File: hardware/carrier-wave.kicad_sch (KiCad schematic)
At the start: 26 parts, among them J1 USB C 2.0, U1 ATSAMD21E18A-M

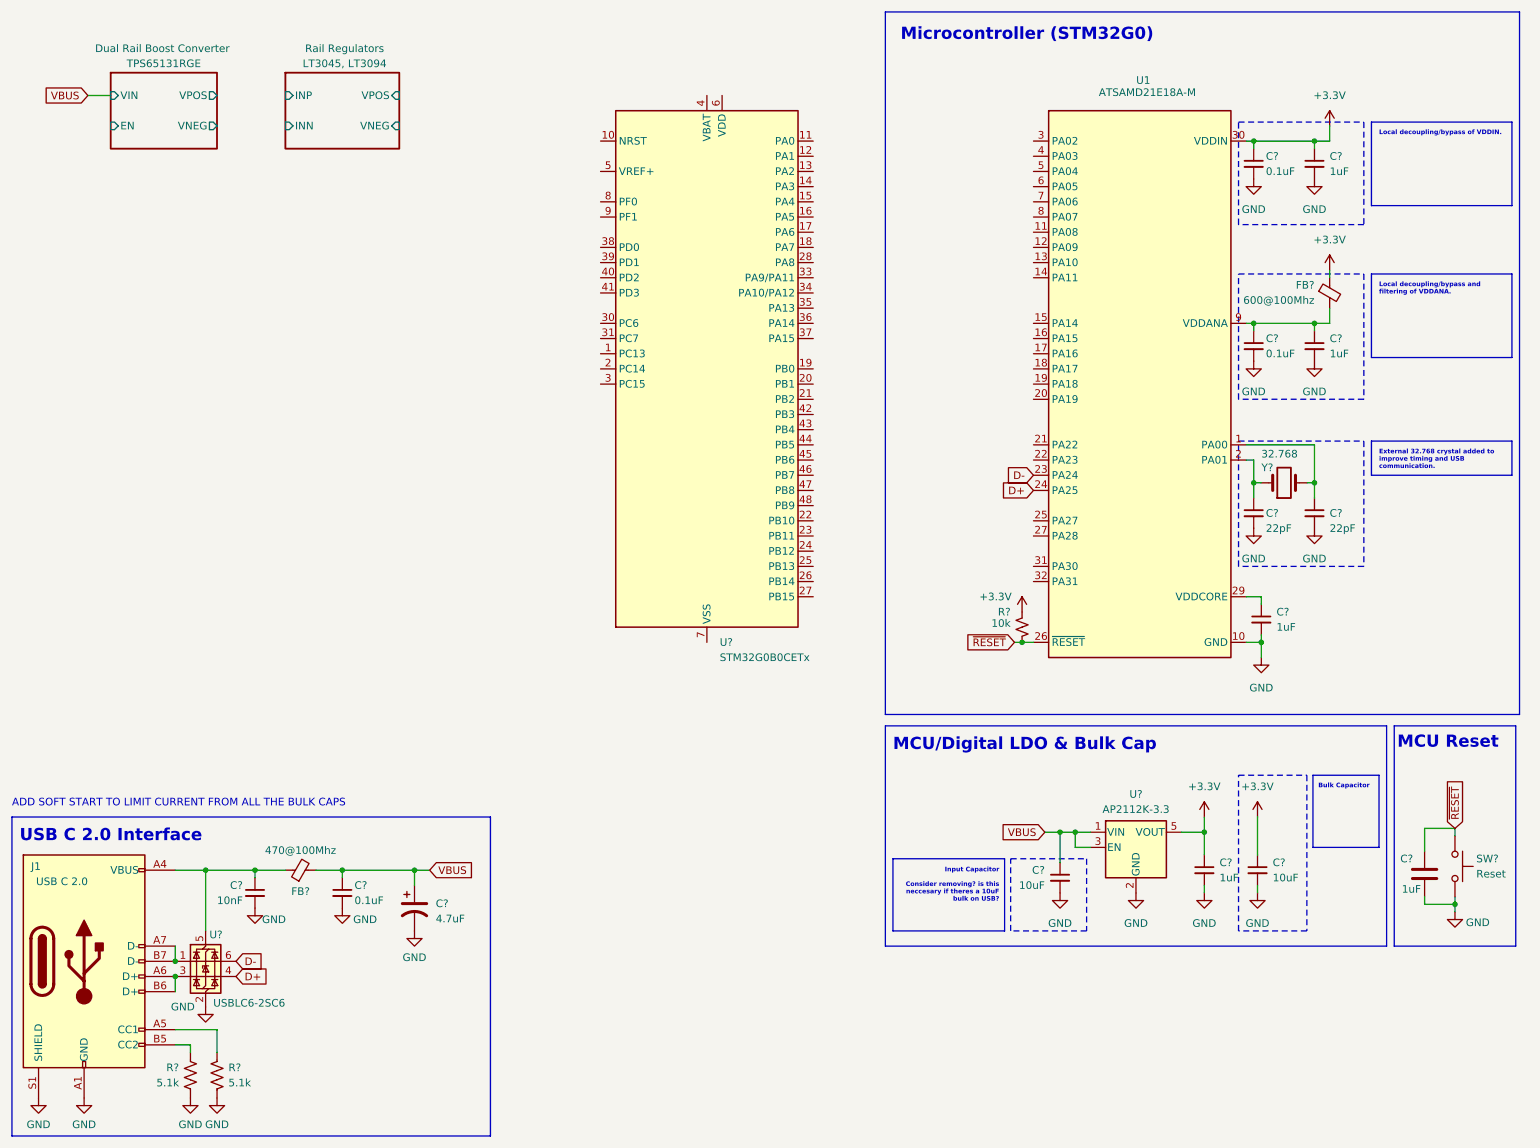
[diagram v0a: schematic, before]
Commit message: Updated Schematic Components
Added AD9834, STM32G0, Op Amps, and potential new voltage regulators
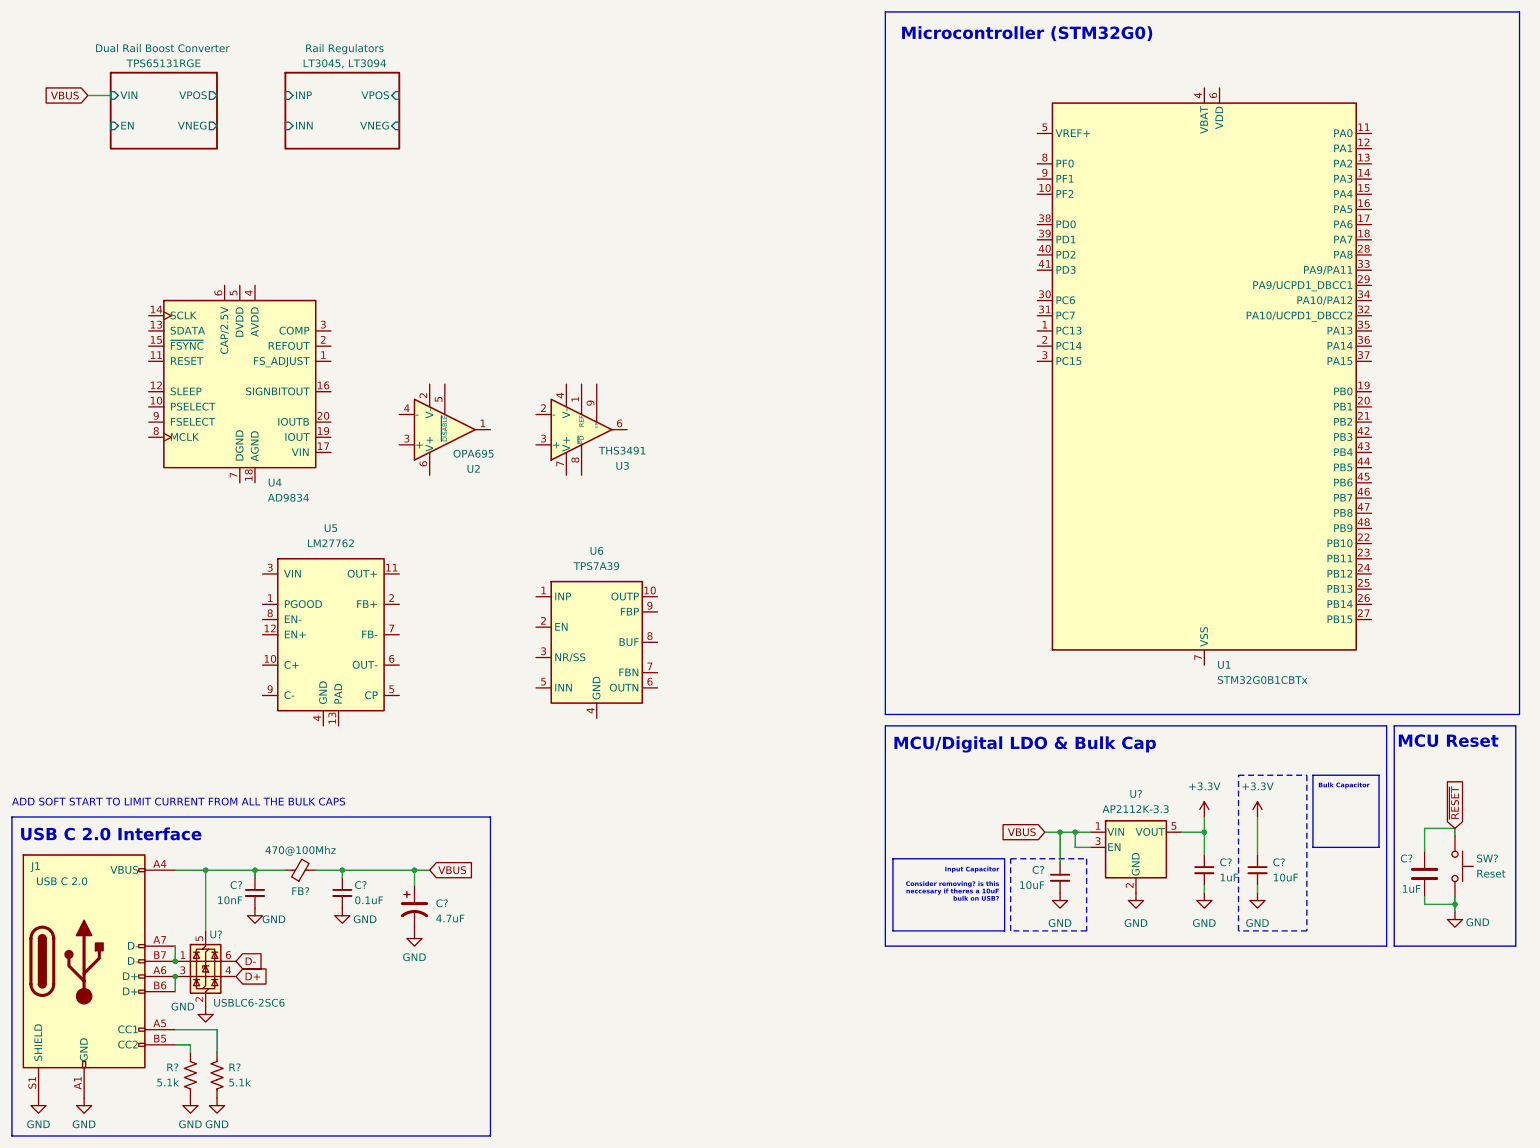
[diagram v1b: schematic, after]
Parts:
- removed C? (x2): 22pF, symbol Device:C_Small
- removed C? (x3): 1uF, symbol Device:C_Small
- removed C? (x2): 0.1uF, symbol Device:C_Small
- removed FB?: 600@100Mhz, Inductor_SMD:L_0603_1608Metric, symbol Device:FerriteBead_Small
- removed R?: 10k, symbol Device:R_Small_US
- removed U1: ATSAMD21E18A-M, Package_DFN_QFN:QFN-32-1EP_5x5mm_P0.5mm_EP3.6x3.6mm, symbol MCU_Microchip_SAMD:ATSAMD21E18A-M
- removed U?: STM32G0B0CETx, Package_QFP:LQFP-48_7x7mm_P0.5mm, symbol MCU_ST_STM32G0:STM32G0B0CETx
- removed Y?: 32.768, symbol Device:Crystal
- added U1: STM32G0B1CBTx, Package_QFP:LQFP-48_7x7mm_P0.5mm, symbol MCU_ST_STM32G0:STM32G0B1CBTx
- added U2: OPA695, Package_TO_SOT_SMD:SOT-23-6, symbol carrier-wave:OPA695
- added U3: THS3491, Package_SO:Texas_R-PDSO-G8_EP2.95x4.9mm_Mask2.4x3.1mm_ThermalVias, symbol Amplifier_Operational:THS3491xDDA
- added U4: AD9834, Package_SO:TSSOP-20_4.4x6.5mm_P0.65mm, symbol Interface:AD9834
- added U5: LM27762, Package_SON:WSON-12-1EP_3x2mm_P0.5mm_EP1x2.65_ThermalVias, symbol Regulator_SwitchedCapacitor:LM27762
- added U6: TPS7A39, Package_SON:Texas_S-PVSON-N10_ThermalVias, symbol Regulator_Linear:TPS7A39
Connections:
- new net: U6.11 (GND), U6.4 (GND)
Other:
- note removed: "External 32.768 crystal added to improve timing and USB communication."
- note removed: "Local decoupling/bypass and filtering of VDDANA."
- note removed: "Local decoupling/bypass of VDDIN."

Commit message: Configure schematic & layout
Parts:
- added U7: TS5A3159ADCK, Package_TO_SOT_SMD:SOT-363_SC-70-6, symbol Analog_Switch:TS5A3159ADCK
- gave numbers to parts that had none: 1
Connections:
- net USB_CC2: now reaches J1.B5 (CC2), R?.1
- net USB_CC1: now reaches J1.A5 (CC1), R?.1
- net D+ renamed USB_D+
- net D- renamed USB_D-
- net VBUS renamed VBUSF
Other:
- removed sheet Rail Regulators
- moved on the sheet: C?, D?, J1, R?, SW?, U5, U6

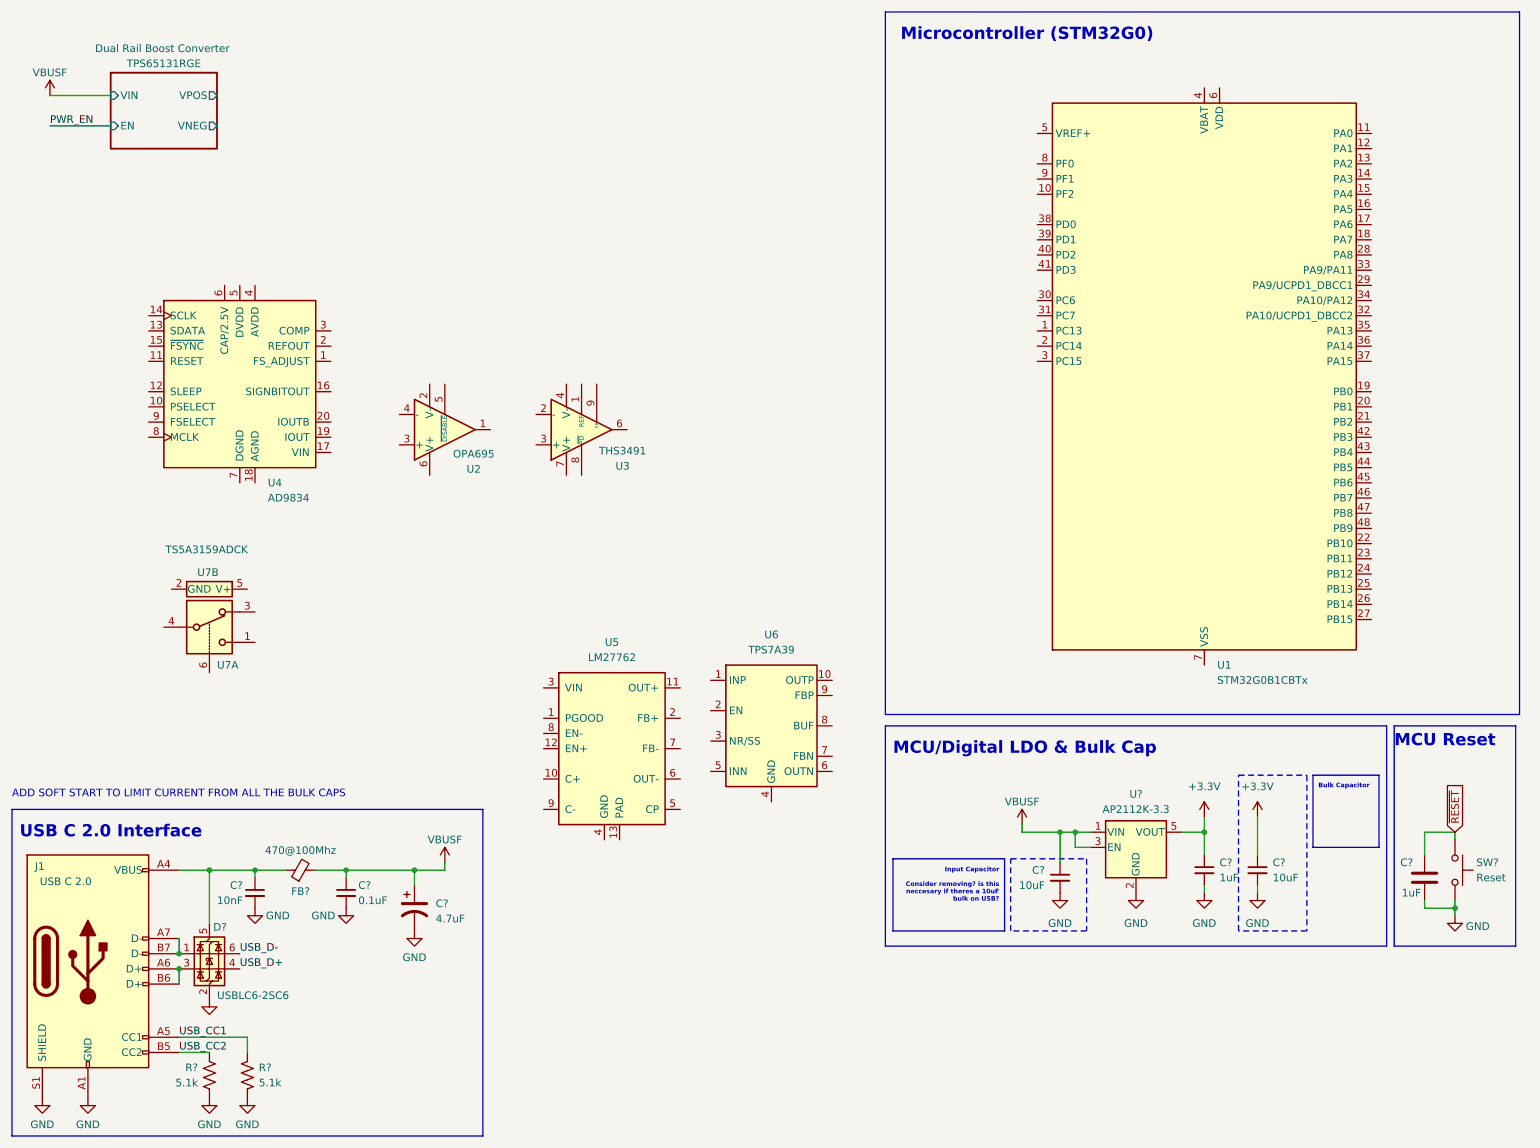
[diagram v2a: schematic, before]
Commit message: Add +/-12V LDOs symbols
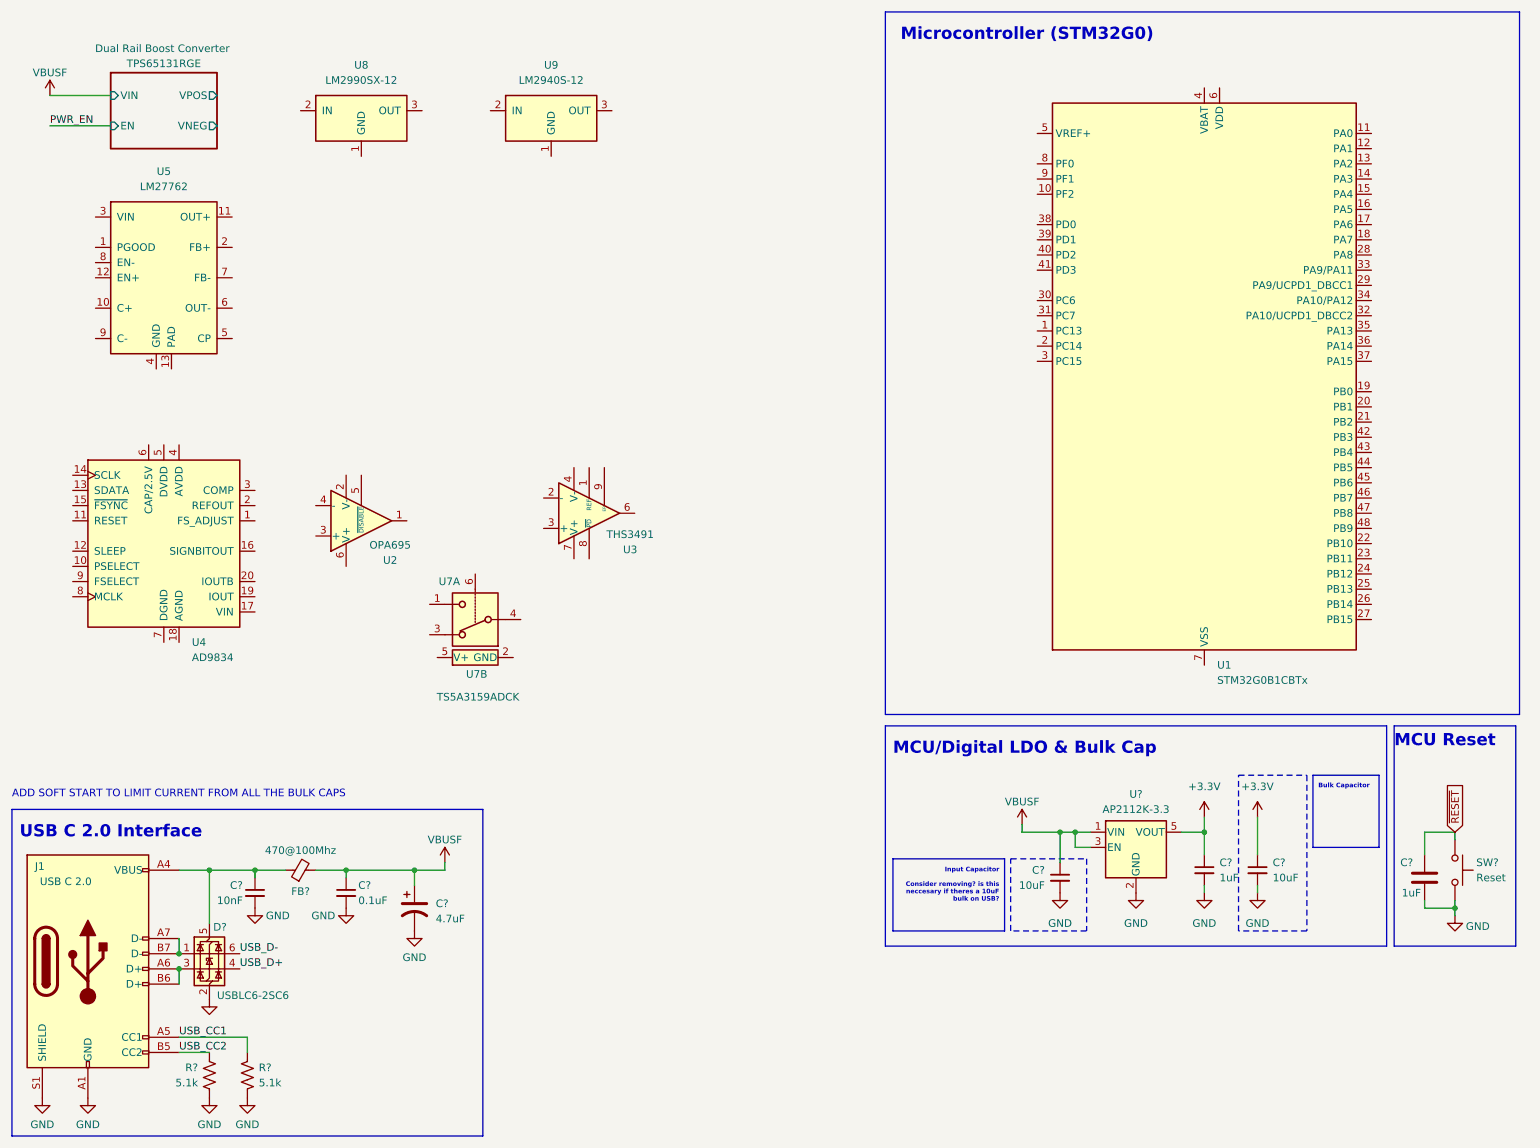
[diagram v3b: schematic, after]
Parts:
- removed U6: TPS7A39, Package_SON:Texas_S-PVSON-N10_ThermalVias, symbol Regulator_Linear:TPS7A39
- added U8: LM2990SX-12, Package_TO_SOT_SMD:TO-263-3_TabPin2, symbol Regulator_Linear:LM2990SX-12
- added U9: LM2940S-12, Package_TO_SOT_SMD:TO-263-3_TabPin2, symbol Regulator_Linear:LM2990SX-12
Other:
- moved on the sheet: U2, U3, U4, U5, U7A, U7B
